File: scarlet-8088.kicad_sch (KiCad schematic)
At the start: 9 parts

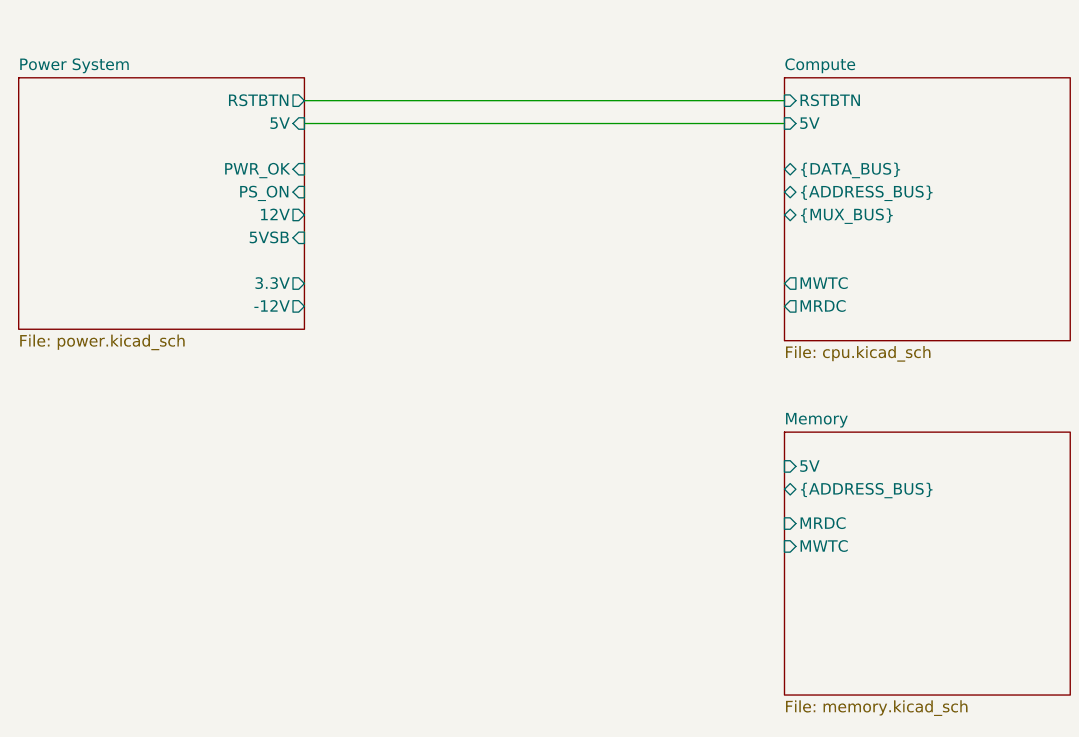
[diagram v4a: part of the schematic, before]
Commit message: Complete UART connection
Signed-off-by: Lucy Mielke <user@domain.tld>
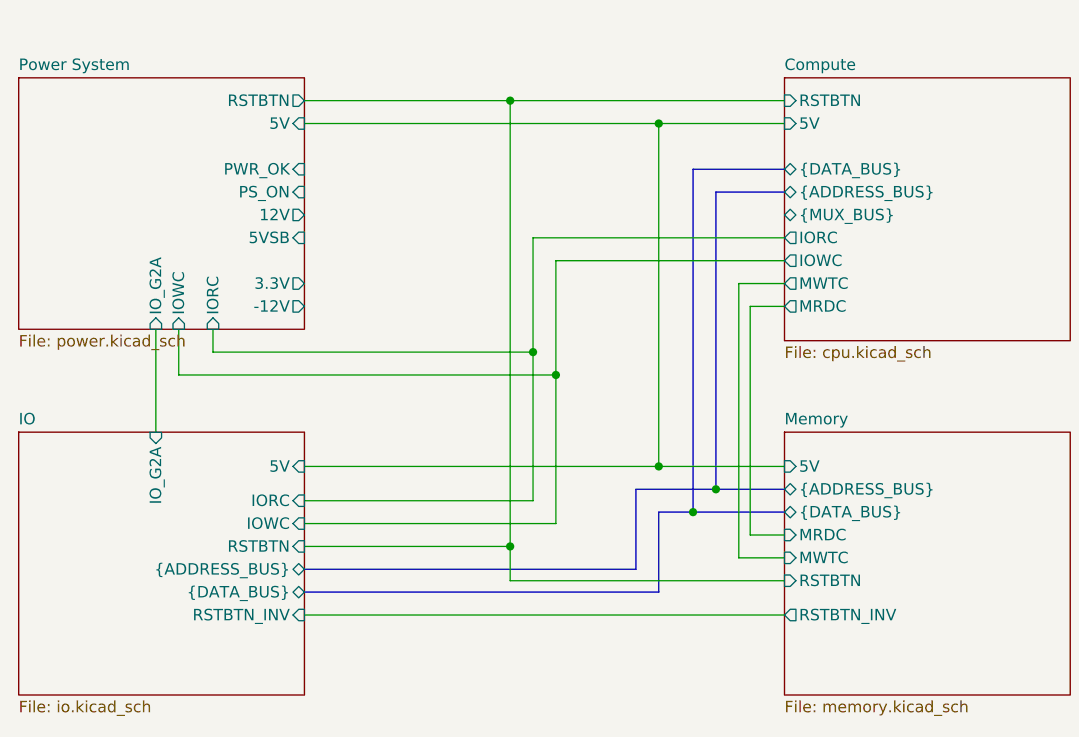
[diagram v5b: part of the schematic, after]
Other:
- added sheet IO (io.kicad_sch)
- sheet Compute ports: added IORC, IOWC; removed none
- sheet Memory ports: added RSTBTN, RSTBTN_INV, {DATA_BUS}; removed none
- sheet Power System ports: added IORC, IOWC, IO_G2A; removed none

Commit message: reorganise
Signed-off-by: Lucy Mielke <user@domain.tld>
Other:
- sheet Compute ports: added INTA, INTR; removed none
- sheet IO ports: added INTA, INTR; removed none
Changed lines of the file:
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@@
 	(wire
 		(pts
+			(xy 81.28 26.67) (xy 81.28 81.28)
+		)
+		(stroke
+			(width 0)
+			(type default)
+		)
+	)
+	(wire
+		(pts
+			(xy 83.82 83.82) (xy 48.26 83.82)
+		)
+		(stroke
+			(width 0)
+			(type default)
+		)
+	)
+	(wire
+		(pts
 			(xy 48.26 24.13) (xy 87.63 24.13)
 		)
@@
 	(wire
 		(pts
+			(xy 81.28 26.67) (xy 101.6 26.67)
+		)
+		(stroke
+			(width 0)
+			(type default)
+		)
+	)
+	(wire
+		(pts
 			(xy 87.63 62.23) (xy 87.63 24.13)
 		)
@@
 		)
 	)
+	(wire
+		(pts
+			(xy 83.82 46.99) (xy 83.82 83.82)
+		)
+		(stroke
+			(width 0)
+			(type default)
+		)
+	)
 	(bus
 		(pts
@@
 		)
 	)
+	(wire
+		(pts
+			(xy 48.26 81.28) (xy 81.28 81.28)
+		)
+		(stroke
+			(width 0)
+			(type default)
+		)
+	)
 	(bus
 		(pts
@@
 		(pts
 			(xy 48.26 62.23) (xy 87.63 62.23)
+		)
+		(stroke
+			(width 0)
+			(type default)
+		)
+	)
+	(wire
+		(pts
+			(xy 101.6 46.99) (xy 83.82 46.99)
 		)
 		(stroke
@@
 			)
 		)
+		(pin "INTA" output
+			(at 48.26 81.28 0)
+			(effects
+				(font
+					(size 1.27 1.27)
+				)
+				(justify right)
+			)
+		)
+		(pin "INTR" input
+			(at 48.26 83.82 0)
+			(effects
+				(font
+					(size 1.27 1.27)
+				)
+				(justify right)
+			)
+		)
 		(pin "RSTBTN_INV" input
 			(at 48.26 78.74 0)
@@
 			(effects
 				(font
+					(size 1.27 1.27)
+				)
+				(justify left)
+			)
+		)
+		(pin "INTA" input
+			(at 101.6 26.67 180)
+			(effects
+				(font
+					(size 1.27 1.27)
+				)
+				(justify left)
+			)
+		)
+		(pin "INTR" output
+			(at 101.6 46.99 180)
+			(effects
+				(font

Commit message: add PIT
Signed-off-by: Lucy Mielke <user@domain.tld>
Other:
- sheet Compute ports: added PCLK; removed none
- sheet IO ports: added ISA0_IRQ, ISA1_IRQ, ISA2_IRQ, ISA3_IRQ, PCLK, PS2_IRQ, RTL_IRQ; removed none
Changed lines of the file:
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@@
+	(wire
+		(pts
+			(xy 90.17 111.76) (xy 48.26 111.76)
+		)
+		(stroke
+			(width 0)
+			(type default)
+		)
+	)
 	(wire
 		(pts
@@
 	(wire
 		(pts
+			(xy 90.17 49.53) (xy 90.17 111.76)
+		)
+		(stroke
+			(width 0)
+			(type default)
+		)
+	)
+	(wire
+		(pts
 			(xy 73.66 36.83) (xy 101.6 36.83)
 		)
@@
 		(pts
 			(xy 76.2 39.37) (xy 101.6 39.37)
+		)
+		(stroke
+			(width 0)
+			(type default)
+		)
+	)
+	(wire
+		(pts
+			(xy 101.6 49.53) (xy 90.17 49.53)
 		)
 		(stroke
@@
 	(sheet
 		(at 16.51 58.42)
-		(size 31.75 29.21)
+		(size 31.75 58.42)
 		(exclude_from_sim no)
 		(in_bom yes)
@@
 		)
 		(property "Sheetfile" "io.kicad_sch"
-			(at 16.51 88.2146 0)
+			(at 16.51 117.4246 0)
 			(show_name no)
 			(do_not_autoplace no)
@@
 		(pin "RSTBTN_INV" input
 			(at 48.26 78.74 0)
+			(effects
+				(font
+					(size 1.27 1.27)
+				)
+				(justify right)
+			)
+		)
+		(pin "ISA0_IRQ" input
+			(at 48.26 93.98 0)
+			(effects
+				(font
+					(size 1.27 1.27)
+				)
+				(justify right)
+			)
+		)
+		(pin "ISA1_IRQ" input
+			(at 48.26 96.52 0)
+			(effects
+				(font
+					(size 1.27 1.27)
+				)
+				(justify right)
+			)
+		)
+		(pin "ISA2_IRQ" input
+			(at 48.26 99.06 0)
+			(effects
+				(font
+					(size 1.27 1.27)
+				)
+				(justify right)
+			)
+		)
+		(pin "ISA3_IRQ" input
+			(at 48.26 101.6 0)
+			(effects
+				(font
+					(size 1.27 1.27)
+				)
+				(justify right)
+			)
+		)
+		(pin "PS2_IRQ" input
+			(at 48.26 104.14 0)
+			(effects
+				(font
+					(size 1.27 1.27)
+				)
+				(justify right)
+			)
+		)
+		(pin "RTL_IRQ" input
+			(at 48.26 106.68 0)
+			(effects
+				(font
+					(size 1.27 1.27)
+				)
+				(justify right)
+			)
+		)
+		(pin "PCLK" input
+			(at 48.26 111.76 0)
 			(effects
 				(font
@@
 	(sheet
 		(at 101.6 19.05)
-		(size 31.75 29.21)
+		(size 31.75 34.29)
 		(exclude_from_sim no)
 		(in_bom yes)
@@
 		)
 		(property "Sheetfile" "cpu.kicad_sch"
-			(at 101.6 48.8446 0)
+			(at 101.6 53.9246 0)
 			(show_name no)
 			(do_not_autoplace no)
@@
 			(effects
 				(font
+					(size 1.27 1.27)
+				)
+				(justify left)
+			)
+		)
+		(pin "PCLK" output
+			(at 101.6 49.53 180)
+			(effects
+				(font

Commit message: PS/2 Controller and connections
Signed-off-by: Lucy Mielke <user@domain.tld>
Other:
- sheet IO ports: added PS2_KBD_IRQ, PS2_MOUSE_IRQ; removed ISA0_IRQ, PS2_IRQ
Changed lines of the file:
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@@
-			)
-		)
-		(pin "ISA0_IRQ" input
-			(at 48.26 93.98 0)
-			(effects
-				(font
-					(size 1.27 1.27)
-				)
-				(justify right)
 			)
 		)
@@
 			)
 		)
-		(pin "PS2_IRQ" input
-			(at 48.26 104.14 0)
-			(effects
-				(font
-					(size 1.27 1.27)
-				)
-				(justify right)
-			)
-		)
 		(pin "RTL_IRQ" input
 			(at 48.26 106.68 0)
@@
 			(effects
 				(font
+					(size 1.27 1.27)
+				)
+				(justify right)
+			)
+		)
+		(pin "PS2_KBD_IRQ" input
+			(at 48.26 86.36 0)
+			(effects
+				(font
+					(size 1.27 1.27)
+				)
+				(justify right)
+			)
+		)
+		(pin "PS2_MOUSE_IRQ" input
+			(at 48.26 88.9 0)
+			(effects
+				(font
